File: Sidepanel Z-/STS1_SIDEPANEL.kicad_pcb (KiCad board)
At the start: 4 copper layers, 82.8 x 100 mm, 32 parts, among them IC1 TMP112AQDRLRQ1, J1 Conn_01x18, J3 Conn_01x12, U1 GUVA-C32SM, U11 INA180A4

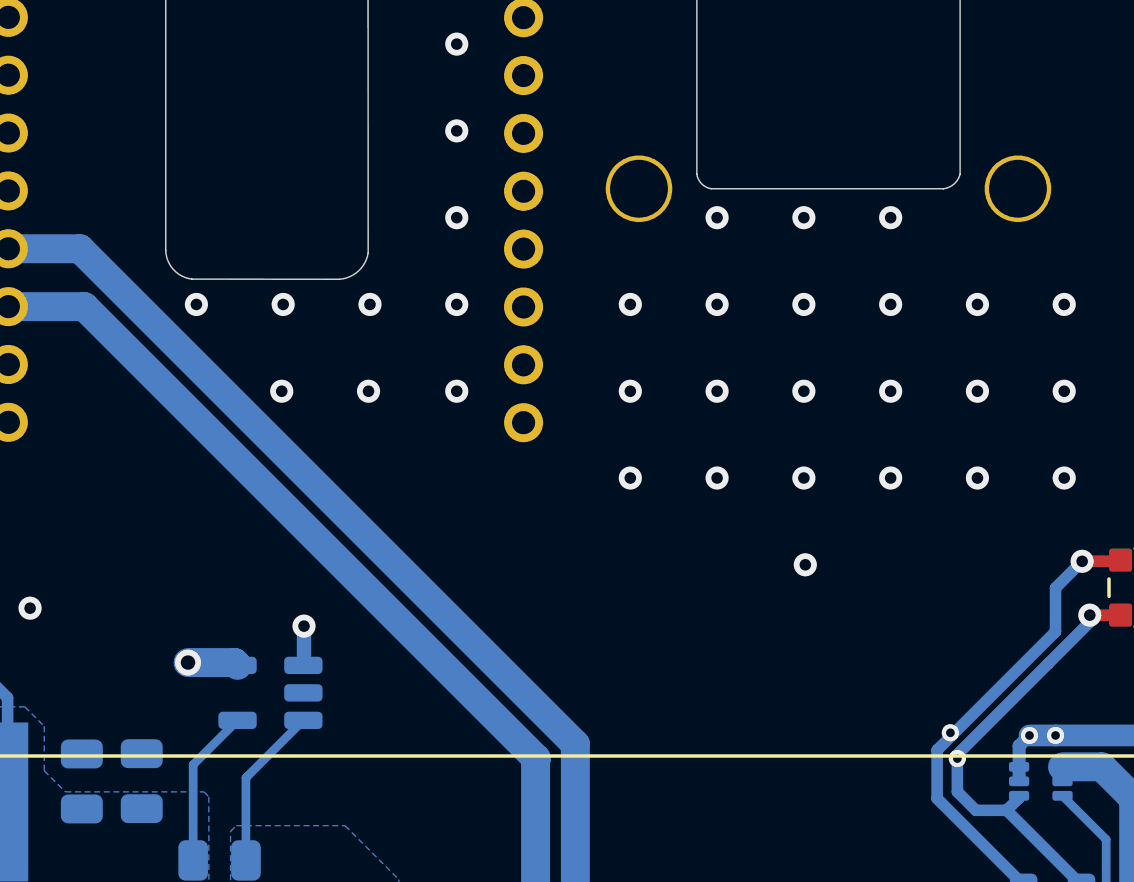
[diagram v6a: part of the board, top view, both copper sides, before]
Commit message: Changed one of the inputs capacitors for all panels with one of 1 uF and lower ESR and moved some traces that were under the inductor.
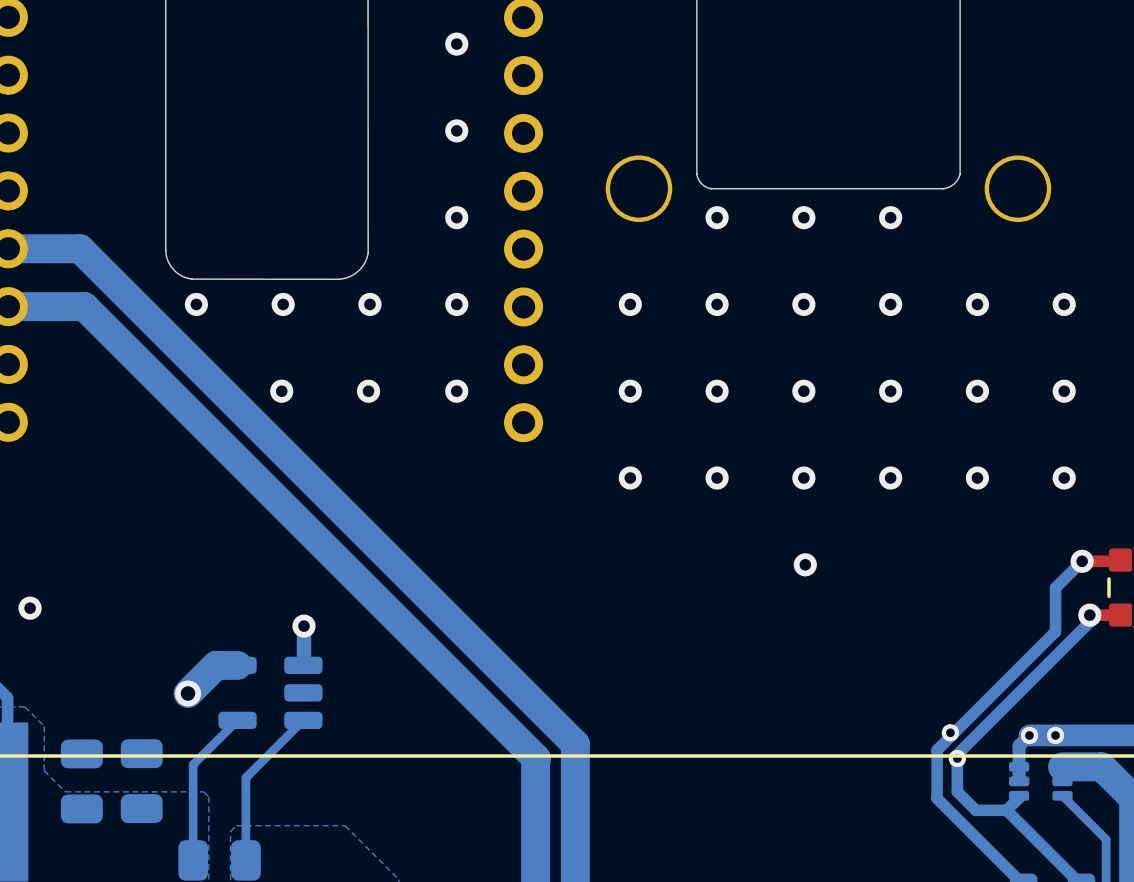
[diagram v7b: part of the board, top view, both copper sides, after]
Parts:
- C61: value 22u -> 1u
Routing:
- net /MPPT1: track 97.5 -> 108.0 mm
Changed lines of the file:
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@@
 	(net 52 "unconnected-(J1-Pin_18-PadS2)")
 	(net 53 "unconnected-(J1-Pin_12-Pad12)")
-	(net 54 "unconnected-(cam1-26-PadMP3)")
+	(net 54 "unconnected-(cam1-23-PadMP1)_1")
 	(net 55 "unconnected-(cam1-23-PadMP1)")
-	(net 56 "unconnected-(cam1-25-PadMP4)")
+	(net 56 "unconnected-(cam1-24-PadMP2)_1")
 	(net 57 "unconnected-(cam1-24-PadMP2)")
 	(footprint "STS_solder:3G30A_40x80"
@@
 		(fp_arc
 			(start 1.842927 -23.275957)
-			(mid 1.206596 -23.605055)
+			(mid 1.206595 -23.605056)
 			(end 0.94 -24.27)
 			(stroke
@@
 		(fp_arc
 			(start 7.937653 -24.17174)
-			(mid 7.594355 -23.548799)
+			(mid 7.594358 -23.548794)
 			(end 6.94 -23.27)
 			(stroke
@@
 		(fp_arc
 			(start 28.4 -26.9)
-			(mid 28.190721 -26.563683)
+			(mid 28.190734 -26.56367)
 			(end 27.83 -26.4)
 			(stroke
@@
 			)
 		)
-		(property "Value_1" "524352271"
+		(property "Value_1" "54548-2271"
 			(at 0 0 0)
 			(unlocked yes)
@@
 			)
 		)
-		(property "Footprint_1" "524352271"
+		(property "Footprint_1" "545482271"
 			(at 0 0 0)
 			(unlocked yes)
@@
 			)
 		)
-		(property "Datasheet_1" "https://www.molex.com/en-us/products/part-detail-pdf/524352271?display=pdf"
+		(property "Datasheet_1" "http://www.molex.com/webdocs/datasheets/pdf/en-us//0545482271_FFC_FPC_CONNECTORS.pdf"
 			(at 0 0 0)
 			(unlocked yes)
@@
 			(size 1.1 2.2)
 			(layers "B.Cu" "B.Paste" "B.Mask")
-			(net 55 "unconnected-(cam1-23-PadMP1)")
+			(net 54 "unconnected-(cam1-23-PadMP1)_1")
 			(pinfunction "23")
 			(pintype "passive+no_connect")
@@
 			(size 1.3 3.05)
 			(layers "B.Cu" "B.Paste" "B.Mask")
-			(net 54 "unconnected-(cam1-26-PadMP3)")
-			(pinfunction "26")
+			(net 55 "unconnected-(cam1-23-PadMP1)")
+			(pinfunction "23")
 			(pintype "passive+no_connect")
 		)
@@
 			(size 1.3 3.05)
 			(layers "B.Cu" "B.Paste" "B.Mask")
-			(net 56 "unconnected-(cam1-25-PadMP4)")
-			(pinfunction "25")
+			(net 57 "unconnected-(cam1-24-PadMP2)")
+			(pinfunction "24")
 			(pintype "passive+no_connect")
 		)
@@
 			(size 1.1 2.2)
 			(layers "B.Cu" "B.Paste" "B.Mask")
-			(net 57 "unconnected-(cam1-24-PadMP2)")
+			(net 56 "unconnected-(cam1-24-PadMP2)_1")
 			(pinfunction "24")
 			(pintype "passive+no_connect")
@@
 			)
 		)
-		(property "Value" "22u"
+		(property "Value" "1u"
 			(at 0 -1.68 90)
 			(layer "B.Fab")
@@
 			)
 		)
-		(property "Description" ""
+		(property "Description" "TMK212B7105KGHTR"
 			(at 0 0 90)
 			(unlocked yes)
@@
 	)
 	(via
-		(at 126.71 79.48)
+		(at 126.71 80.55)
 		(size 0.9)
 		(drill 0.5)
@@
 	)
 	(segment
+		(start 110.405 96.89)
+		(end 107.175 93.66)
+		(width 1)
+		(layer "In2.Cu")
+		(net 10)
+	)
+	(segment
 		(start 110 89.85)
 		(end 109.975 89.825)
@@
 	)
 	(segment
-		(start 112.53 93.66)
-		(end 107.175 93.66)
-		(width 1)
-		(layer "In2.Cu")
-		(net 10)
-	)
-	(segment
 		(start 99.35 90.45)
 		(end 100.37 91.47)
@@
 	)
 	(segment
+		(start 123.86 96.89)
+		(end 110.405 96.89)
+		(width 1)
+		(layer "In2.Cu")
+		(net 10)
+	)
+	(segment
 		(start 110 90.9)
 		(end 110 89.85)
@@
 	)
 	(segment
-		(start 126.71 79.48)
-		(end 112.53 93.66)
+		(start 126.71 94.04)
+		(end 123.86 96.89)
 		(width 1)
 		(layer "In2.Cu")
@@
 	)
 	(segment
+		(start 126.71 80.55)
+		(end 126.71 94.04)
+		(width 1)
+		(layer "In2.Cu")
+		(net 10)
+	)
+	(segment
 		(start 109.385 95.3)
 		(end 109.1 95.585)
@@
 	)
 	(segment
-		(start 128.325 79.48)
-		(end 128.4225 79.5775)
-		(width 1)
-		(layer "B.Cu")
-		(net 10)
-	)
-	(segment
 		(start 112.275 122.375)
 		(end 114.125 122.375)
@@
 	)
 	(segment
-		(start 126.71 79.48)
-		(end 128.325 79.48)
-		(width 1)
-		(layer "B.Cu")
-		(net 10)
-	)
-	(segment
 		(start 103.72 91.02)
 		(end 105.265 92.565)
@@
 	)
 	(segment
+		(start 127.6825 79.5775)
+		(end 128.4225 79.5775)
+		(width 1)
+		(layer "B.Cu")
+		(net 10)
+	)
+	(segment
 		(start 103.72 90.345)
 		(end 103.72 91.02)
@@
 		(layer "B.Cu")
 		(net 10)
+	)
+	(segment
+		(start 126.71 80.55)
+		(end 127.6825 79.5775)
+		(width 1)
+		(layer "B.Cu")
+		(net 10)

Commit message: generated the gerber files for ordering
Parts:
- added ?: , , F.Cu at (103.4, 83.9)
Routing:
- net /MPPT1: track 108.0 -> 109.2 mm
- net GND1: track 107.9 -> 108.8 mm
- net /SDA: track 114.4 -> 115.2 mm
